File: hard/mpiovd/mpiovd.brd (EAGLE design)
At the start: 230 x 150 mm, 868 parts

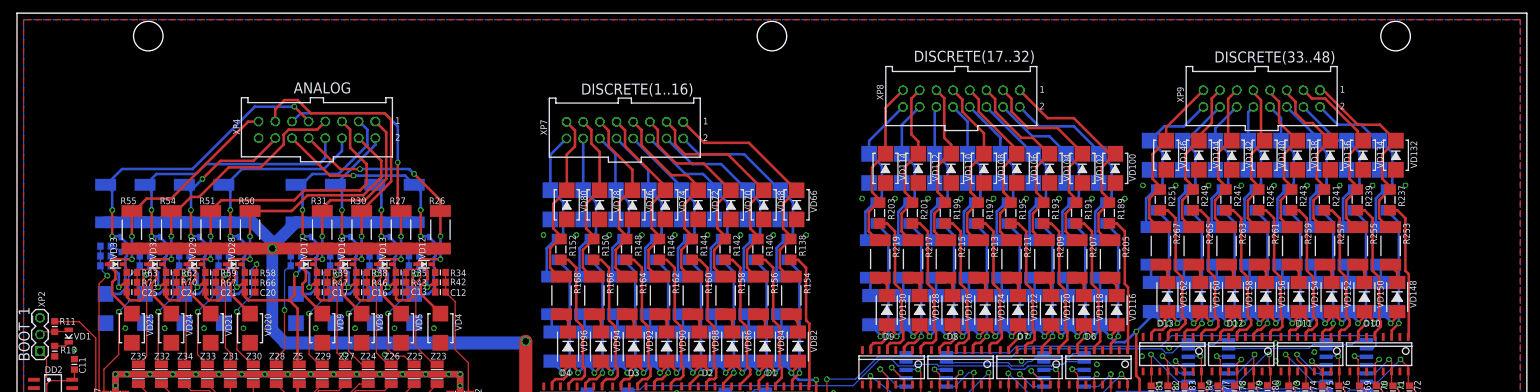
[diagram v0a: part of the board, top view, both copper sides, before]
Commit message: added some symbols
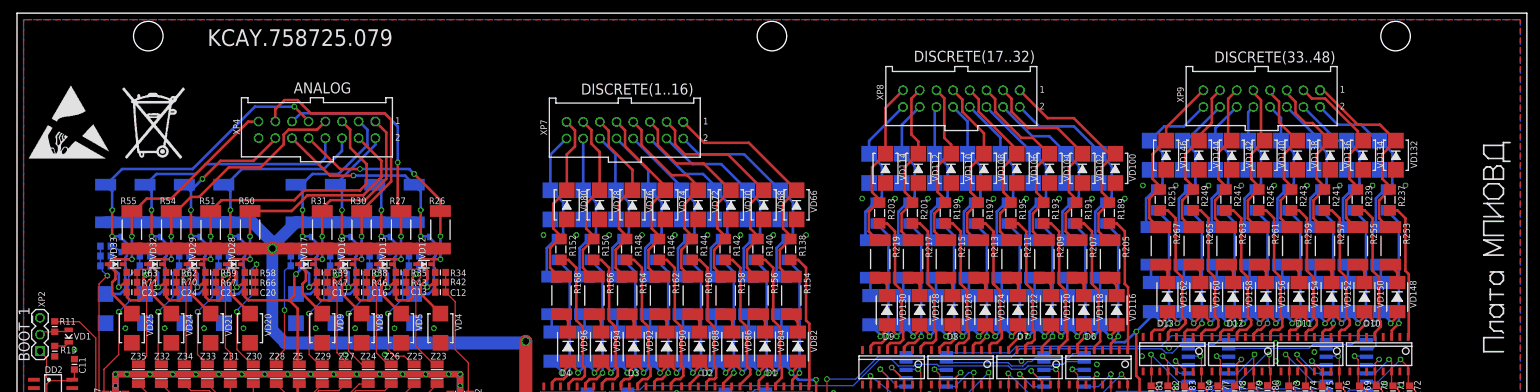
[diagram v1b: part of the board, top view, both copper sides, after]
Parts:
- added U$1: (no value), symbols:STATIC_12
- added U$2: (no value), symbols:NOT_RECYCLE_12
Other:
- board text added: "KCAY.758725.079"

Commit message: nop
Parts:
- added U$3: (no value), symbols:QR
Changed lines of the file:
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@@
 <element name="U$1" library="symbols" package="STATIC_12" value="" x="8" y="132"/>
 <element name="U$2" library="symbols" package="NOT_RECYCLE_12" value="" x="20" y="133"/>
+<element name="U$3" library="symbols" package="QR" value="" x="79.9" y="129.5" rot="MR0"/>
 </elements>
 <signals>

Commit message: n contr
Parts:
- turned Z10 to 180 degrees
- turned Z11 to 180 degrees
- turned Z17 to 180 degrees
- turned Z2 to 180 degrees
- turned Z3 to 180 degrees
- turned Z4 to 180 degrees
- turned Z5 to 90 degrees
- turned Z6 to 180 degrees
- turned Z7 to 180 degrees
- turned Z8 to 180 degrees
- turned Z9 to 180 degrees
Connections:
- net AGND: now also Z5.3; no longer Z5.1
- net BOOT_0: now also Z10.1; no longer Z10.3
- net BOOT_1: now also Z9.1; no longer Z9.3
- net I2C_SCL: now also Z11.1; no longer Z11.3
- net I2C_SDA: now also Z17.3; no longer Z17.1
- net JTCK: now also Z7.3; no longer Z7.1
- net JTDI: now also Z6.3; no longer Z6.1
- net JTDO: now also Z4.3; no longer Z4.1
- net JTMS: now also Z3.3; no longer Z3.1
- net JTRST: now also Z2.3; no longer Z2.1
- net N$331: now also Z5.1; no longer Z5.3
- net N$332: now also Z10.3; no longer Z10.1
- net N$333: now also Z9.3; no longer Z9.1
- net N$334: now also Z2.1; no longer Z2.3
- net N$335: now also Z6.1; no longer Z6.3
- net N$336: now also Z3.1; no longer Z3.3
- net N$337: now also Z8.1; no longer Z8.3
- net N$338: now also Z7.1; no longer Z7.3
- net N$339: now also Z4.1; no longer Z4.3
- net N$340: now also Z17.1; no longer Z17.3
- net N$341: now also Z11.3; no longer Z11.1
- net RST: now also Z8.3; no longer Z8.1
